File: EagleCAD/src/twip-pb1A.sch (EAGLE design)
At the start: 22 parts, among them J1 UJ2-BH-1-TH

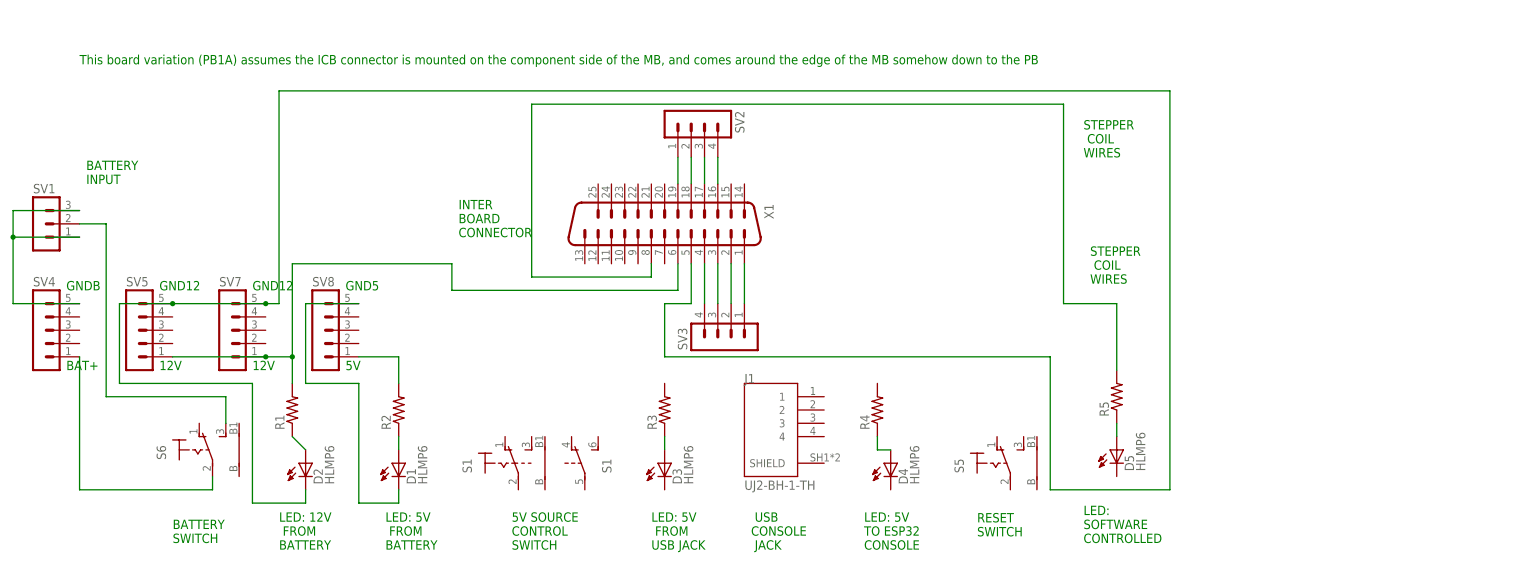
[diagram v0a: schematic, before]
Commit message: Sep 24 checkpoint has mutually consistent versions of MB and PB layouts, and pinouts documentation
completed layout of peripheral board, with a few retrofits to MB for IBC connector changes. Added a 4 position DIP switch to PB as a way to have jumpers that cross other traces, as I couldn't quite do a single sided layout. All switches go to the right when active, and the voltage regulators, whose 4 legs are represented by two 5 pin headers, are correctly scaled. I'd like to space out the top connector for the stepper motor connections, but the board is at the max size allowed, and Eagle CAD won't allow it to be moved upward.
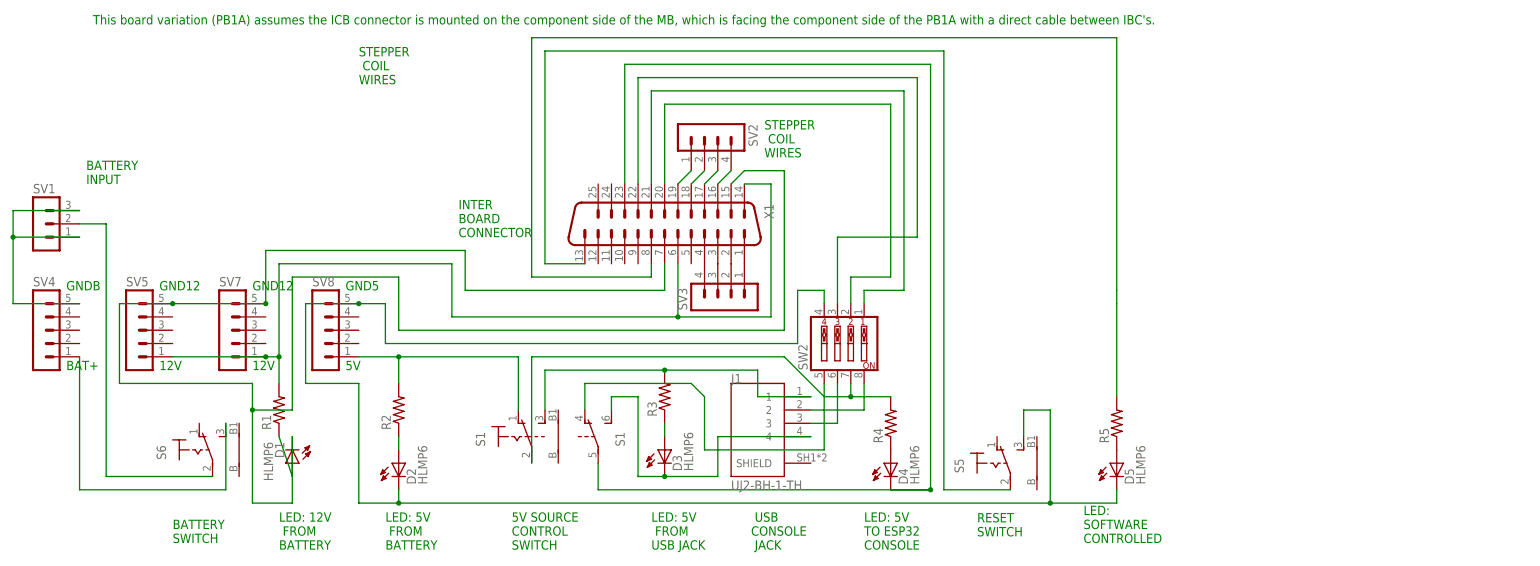
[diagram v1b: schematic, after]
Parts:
- added SW2: (no value), special:SW_DIP-4
- R1, R2, R3, R4, R5: device resistor:R-US_0207/15 -> resistor:R-US_0207/5V
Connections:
- new net N$22: R4.2, S11.P, SW2.7
- new net N$23: D3.K, J1.4, S1B.S
- new net N$24: SW2.1, X1G$1.21
- new net N$25: SW2.3, X1G$1.22
- new net N$26: SW2.2, X1G$1.20
- new net N$27: D4.K, S1B.P, X1G$1.23
- new net N$28: S5.P, X1G$1.13
- new net N$29: D1.K, SV5.5, SV7.5, X1G$1.15, X1G$1.7
- new net N$30: S1B.O, SW2.5
- new net N$31: D2.K, D5.K, S5.S, SV8.5, SW2.4
- new net N$33: J1.3, SW2.6
- net N$1: now also D1.A; no longer D2.A
- net N$10: now also S6.S; no longer S6.P
- net N$12: now also S11.O
- net N$13: now also J1.2, SW2.8; no longer D1.K, SV8.5
- net N$2: now also D2.A; no longer D1.A
- net N$7: now also S6.P; no longer S6.S
- net N$8: now also X1G$1.14
- net N$9: now also J1.1, R3.2, S11.S; no longer D2.K, SV5.5, SV7.5, X1G$1.5
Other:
- note added: "This board variation (PB1A) assumes the ICB connector is mounted on the component side of the MB, which is facing the component side of the PB1A with a direct cable between IBC's."
- note removed: "This board variation (PB1A) assumes the ICB connector is mounted on the component side of the MB, and comes around the edge of the MB somehow down to the PB"
- moved on the sheet: D1, D2, D3, D5, J1, R1, R3, R4, R5, S1, SV2, SV3
